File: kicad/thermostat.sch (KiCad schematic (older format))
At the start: 27 parts, among them IC1 LM2596S-5, J1 Display i2c, J2 Sensor i2c, J6 Screw_Terminal_01x05

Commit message: first pass at supercap circuit, still WIP
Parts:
- added C1: 25F, Capacitors_THT:CP_Radial_D16.0mm_P7.50mm, symbol Device:CP
- added C2: 2.2uF, Capacitors_SMD:C_0805, symbol Device:C
- added C3: 1nF, Capacitors_SMD:C_0805, symbol Device:C
- added C3: 100uF, Capacitors_SMD:C_0805, symbol Device:C
- added L2: 2.2uH, Inductors_SMD:L_Coilcraft_XAL5030, symbol Device:L
- added R10: 113k, Resistors_SMD:R_0805, symbol Device:R_US
- added R11: 38.3k, Resistors_SMD:R_0805, symbol Device:R_US
- added R12: 1k, Resistors_SMD:R_0805, symbol Device:R_US
- added R13: 348k, Resistors_SMD:R_0805, symbol Device:R_US
- added R14: 698k, Resistors_SMD:R_0805, symbol Device:R_US
- added R15: 1050k, Resistors_SMD:R_0805, symbol Device:R_US
- added R16: 200k, Resistors_SMD:R_0805, symbol Device:R_US
- added R18: 12m, Resistors_SMD:R_0805, symbol Device:R_US
- added U1: LTC4041, project_footprints:ltc4041, symbol thermostat:LTC4041
- added U2: SIR424DP, Housings_SOIC:PowerPAK_SO-8_Single, symbol thermostat:SIR424DP
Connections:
- net labels added: PWR_5V_BACKUP
- net labels removed: TEST
- wire segments 110 -> 149
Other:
- note added: "Need some kind of bypass mechanism"
- moved on the sheet: C1, C2, CONN1, D1, D2, D3, Gr1, IC1, J1, J2, J6, L1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

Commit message: addition of bmp280
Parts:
- added C21: 1uF, Capacitors_SMD:C_0805, symbol Device:C
- added C22: 100nF, Capacitors_SMD:C_0805, symbol Device:C
- added J31: Conn_02x03_Odd_Even, Socket_Strips:Socket_Strip_Straight_2x03_Pitch2.54mm_SMD, symbol Connector_Generic:Conn_02x03_Odd_Even
- added R21, R22, R23, R24: 10k, Resistors_SMD:R_0805, symbol Device:R_US
- added U21: BMP280, Housings_LGA:Bosch_LGA-8_2.5x2.5mm_Pitch0.65mm_ClockwisePinNumbering, symbol Sensor_Pressure:BMP280
- IC1: footprint project_footprints:TO170P1435X465-6N -> TO_SOT_Packages_SMD:TO-263-5_TabPin3
- RELAY1, RELAY2, RELAY3: symbol thermostat:Relay? -> thermostat-rescue:Relay?-thermostat
- U11: renamed from U1; Mouser 584-4041IUFDPB -> 584-4041EUFDPB
- renumbered C1 to C11, C2 to C12, C3 to C13, C3 to C14, U2 to U12
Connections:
- net labels added: PWR_5V_CAP, PWR_5V_CAP_IN, PWR_5V_RAW
- net labels removed: PWR_5V_BACKUP
- wire segments 149 -> 182
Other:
- note added: "Based on https://www.electroschematics.com/bmp280-diy-project-primer/"
- note added: "To bypass supercapacitor circuit, jumper 1,2\nTo enable supercapacitor circuit, jumper 3,4 and 5,6"
- note removed: "Need some kind of bypass mechanism"
- moved on the sheet: C1, C11, C12, C13, C14, C2, D1, D2, D3, Gr1, IC1, L1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

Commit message: updates
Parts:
- removed J2: Sensor i2c, Socket_Strips:Socket_Strip_Straight_1x04_Pitch2.54mm, symbol Connector_Generic:Conn_01x04
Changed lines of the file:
@@
 	1700 1100 1700 750
 Connection ~ 1700 1100
-Text Label 2100 3200 0    50   ~ 0
-GND
 Wire Wire Line
 	2500 2700 2500 3200
@@
 	1800 3000 1800 3200
 Wire Wire Line
-	1800 3200 2500 3200
+	1800 3200 2150 3200
 Text Label 6600 1400 0    50   ~ 0
 HVAC_PWR(RED)
@@
 	1    0    0    -1
 $EndComp
-$Comp
-L Connector_Generic:Conn_01x04 J2
-U 1 1 5D67AFA8
-P 7600 2650
-F 0 "J2" H 7680 2642 50  0000 L CNN
-F 1 "Sensor i2c" H 7680 2551 50  0000 L CNN
-F 2 "Socket_Strips:Socket_Strip_Straight_1x04_Pitch2.54mm" H 7600 2650 50  0001 C CNN
-F 3 "~" H 7600 2650 50  0001 C CNN
-F 4 "99" H 7600 2650 50  0001 C CNN "Populate"
-F 5 "200-SLW10401SS" H 7600 2650 50  0001 C CNN "Mouser"
-	1    7600 2650
-	1    0    0    -1
-$EndComp
 Text Label 7200 2050 2    50   ~ 0
 GND
@@
 Text Label 7200 2350 2    50   ~ 0
 GPIO3(SCL1)
-Text Label 7200 2550 2    50   ~ 0
-GPIO2(SDA1)
-Text Label 7200 2650 2    50   ~ 0
-GPIO3(SCL1)
-Text Label 7200 2750 2    50   ~ 0
-GND
-Text Label 7200 2850 2    50   ~ 0
-PWR_5V
 Wire Wire Line
 	7200 2050 7400 2050
@@
 Wire Wire Line
 	7200 2350 7400 2350
-Wire Wire Line
-	7400 2550 7200 2550
-Wire Wire Line
-	7400 2650 7200 2650
-Wire Wire Line
-	7200 2750 7400 2750
-Wire Wire Line
-	7400 2850 7200 2850
 $Comp
 L thermostat:LM2596S-12-RENUM IC1
@@
 	9400 4450 9500 4450
 Connection ~ 9500 4450
-Text Label 9500 3500 2    50   ~ 0
+Text Label 9500 3400 2    50   ~ 0
 PWR_3.3V
 Text Label 8500 4300 3    50   ~ 0
@@
 	9500 3550 10100 3550
 Wire Wire Line
-	9500 3500 9500 3550
-Wire Wire Line
 	9400 3700 9400 3550
 Connection ~ 9400 3550
@@
 	8500 4300 8500 4000
 Connection ~ 8500 4000
-Text Notes 7750 3400 0    50   ~ 0
+Text Notes 7750 3300 0    50   ~ 0
 Based on https://www.electroschematics.com/bmp280-diy-project-primer/
+$Comp
+L thermostat:GND #PWR?
+U 1 1 5E0DA227
+P 2150 3200
+F 0 "#PWR?" H 2150 2950 50  0001 C CNN
+F 1 "GND" H 2155 3027 50  0000 C CNN
+F 2 "" H 2150 3200 50  0000 C CNN
+F 3 "" H 2150 3200 50  0000 C CNN
+	1    2150 3200
+	1    0    0    -1
+$EndComp
+Wire Wire Line
+	2150 3200 2500 3200
+Connection ~ 2150 3200
+Wire Wire Line
+	9500 3400 9500 3550
 $EndSCHEMATC

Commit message: new symbol for transistor
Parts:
- removed U12: SIR424DP, Housings_SOIC:PowerPAK_SO-8_Single, symbol thermostat:SIR424DP
- added T1: SIR424DP, Housings_SOIC:PowerPAK_SO-8_Single, symbol Transistor_FET:BUK9M9R1-40EX
- U11: symbol thermostat:LTC4041 -> thermostat-rescue:LTC4041-thermostat
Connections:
- net PWR_5V_CAP: now also T1.5 (D)
- net at U11.15 (IGATE): now also T1.4 (G)
- net at R18.1, U11.7 (CLN): now also T1.1 (S), T1.2 (S), T1.3 (S)
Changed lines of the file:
@@
 EESchema Schematic File Version 4
-LIBS:thermostat-cache
-EELAYER 29 0
+EELAYER 30 0
 EELAYER END
 $Descr A4 11693 8268
@@
 	2850 5450 2950 5450
 $Comp
-L thermostat:LTC4041 U11
+L thermostat-rescue:LTC4041-thermostat U11
 U 1 1 5E1374C4
 P 2500 6250
@@
 Wire Wire Line
 	2550 5150 2550 5450
-Connection ~ 2550 5150
 Wire Wire Line
 	2950 5450 3200 5450
 Wire Wire Line
 	3200 5450 3200 5150
-Wire Wire Line
-	3200 5150 3050 5150
 Connection ~ 2950 5450
 Wire Wire Line
 	3200 5150 3400 5150
 Connection ~ 3200 5150
-Wire Wire Line
-	2700 5400 2700 5450
-Wire Wire Line
-	3050 5250 3050 5150
-Connection ~ 3050 5150
-$Comp
-L thermostat:SIR424DP U12
-U 1 1 5E21048A
-P 2900 5200
-F 0 "U12" H 2750 5450 50  0000 L CNN
-F 1 "SIR424DP" H 2600 5350 50  0000 L CNN
-F 2 "Housings_SOIC:PowerPAK_SO-8_Single" V 2750 4950 50  0001 C CNN
-F 3 "https://www.mouser.com/datasheet/2/427/sir424dp-244427.pdf" H 2900 5250 50  0001 C CNN
-F 4 "781-SIR424DP-GE3" V 2850 5200 50  0001 C CNN "Mouser"
-	1    2900 5200
-	1    0    0    -1
-$EndComp
 $Comp
 L Device:R_US R10
@@
 Wire Wire Line
 	9500 3400 9500 3550
+$Comp
+L Transistor_FET:BUK9M9R1-40EX T1
+U 1 1 5E0E0418
+P 2750 5250
+F 0 "T1" V 3092 5250 50  0000 C CNN
+F 1 "SIR424DP" V 3001 5250 50  0000 C CNN
+F 2 "Housings_SOIC:PowerPAK_SO-8_Single" H 2950 5175 50  0001 L CIN
+F 3 "https://www.mouser.com/datasheet/2/427/sir424dp-244427.pdf" V 2750 5250 50  0001 L CNN
+F 4 "781-SIR424DP-GE3" H 2750 5250 50  0001 C CNN "Mouser"
+	1    2750 5250
+	0    1    -1   0
+$EndComp
+Connection ~ 2550 5150
+Wire Wire Line
+	2700 5450 2750 5450
+Wire Wire Line
+	2950 5150 3200 5150
 $EndSCHEMATC

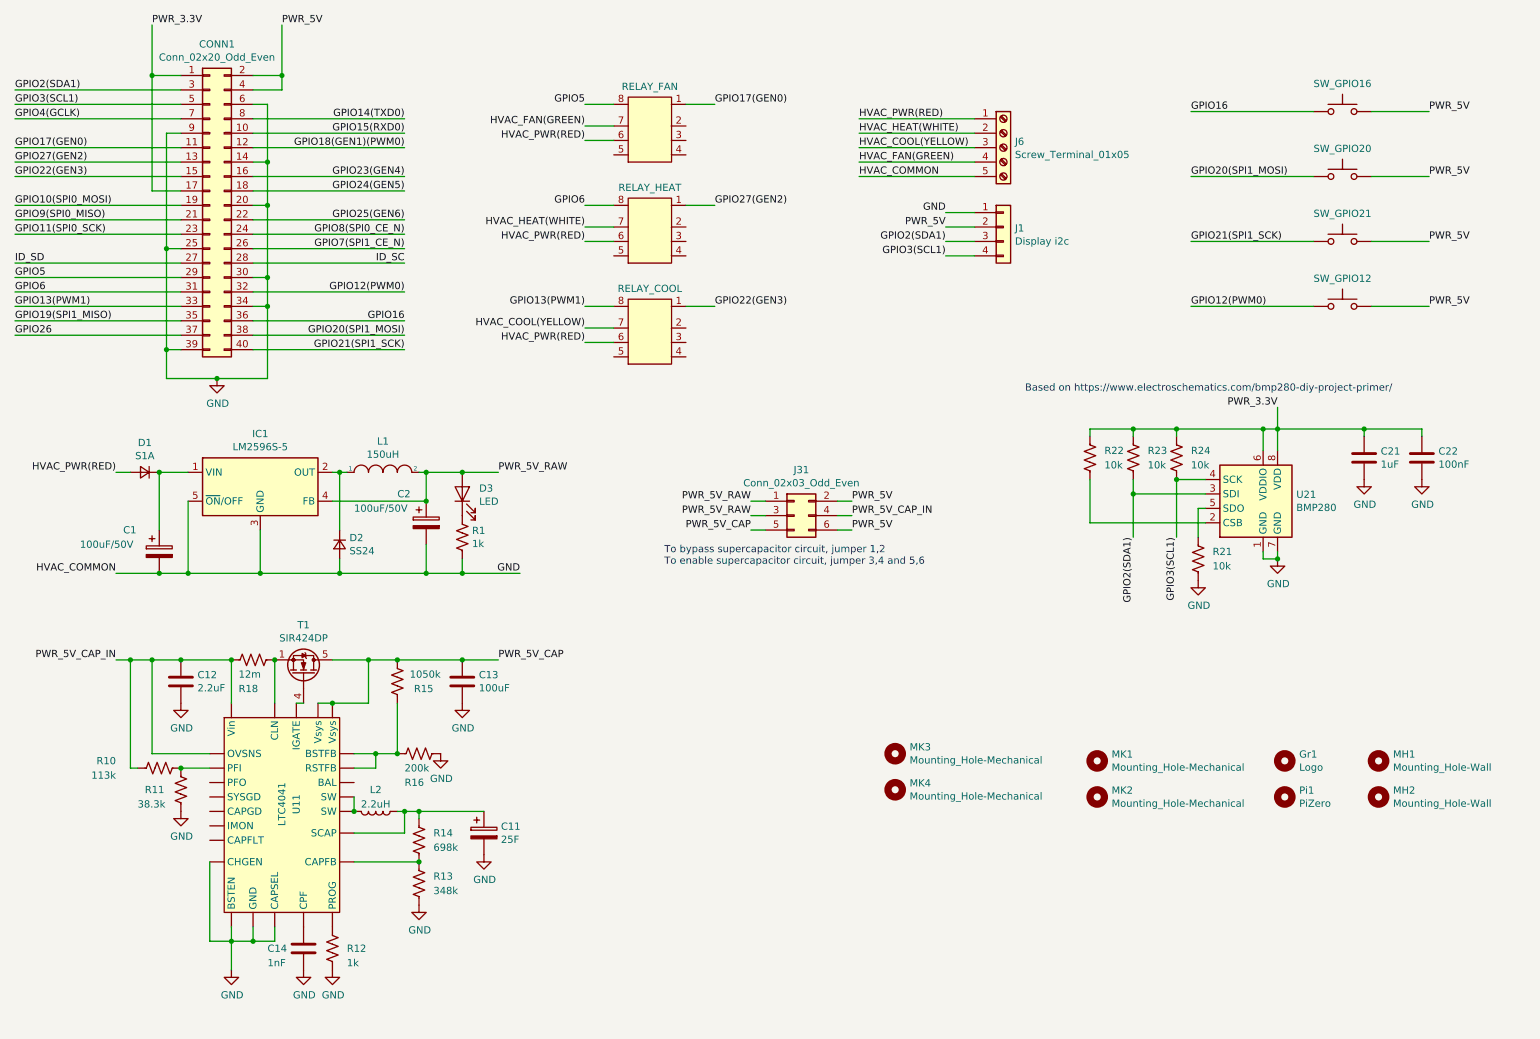
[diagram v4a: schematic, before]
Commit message: Support for KiCad v5.14 libraries
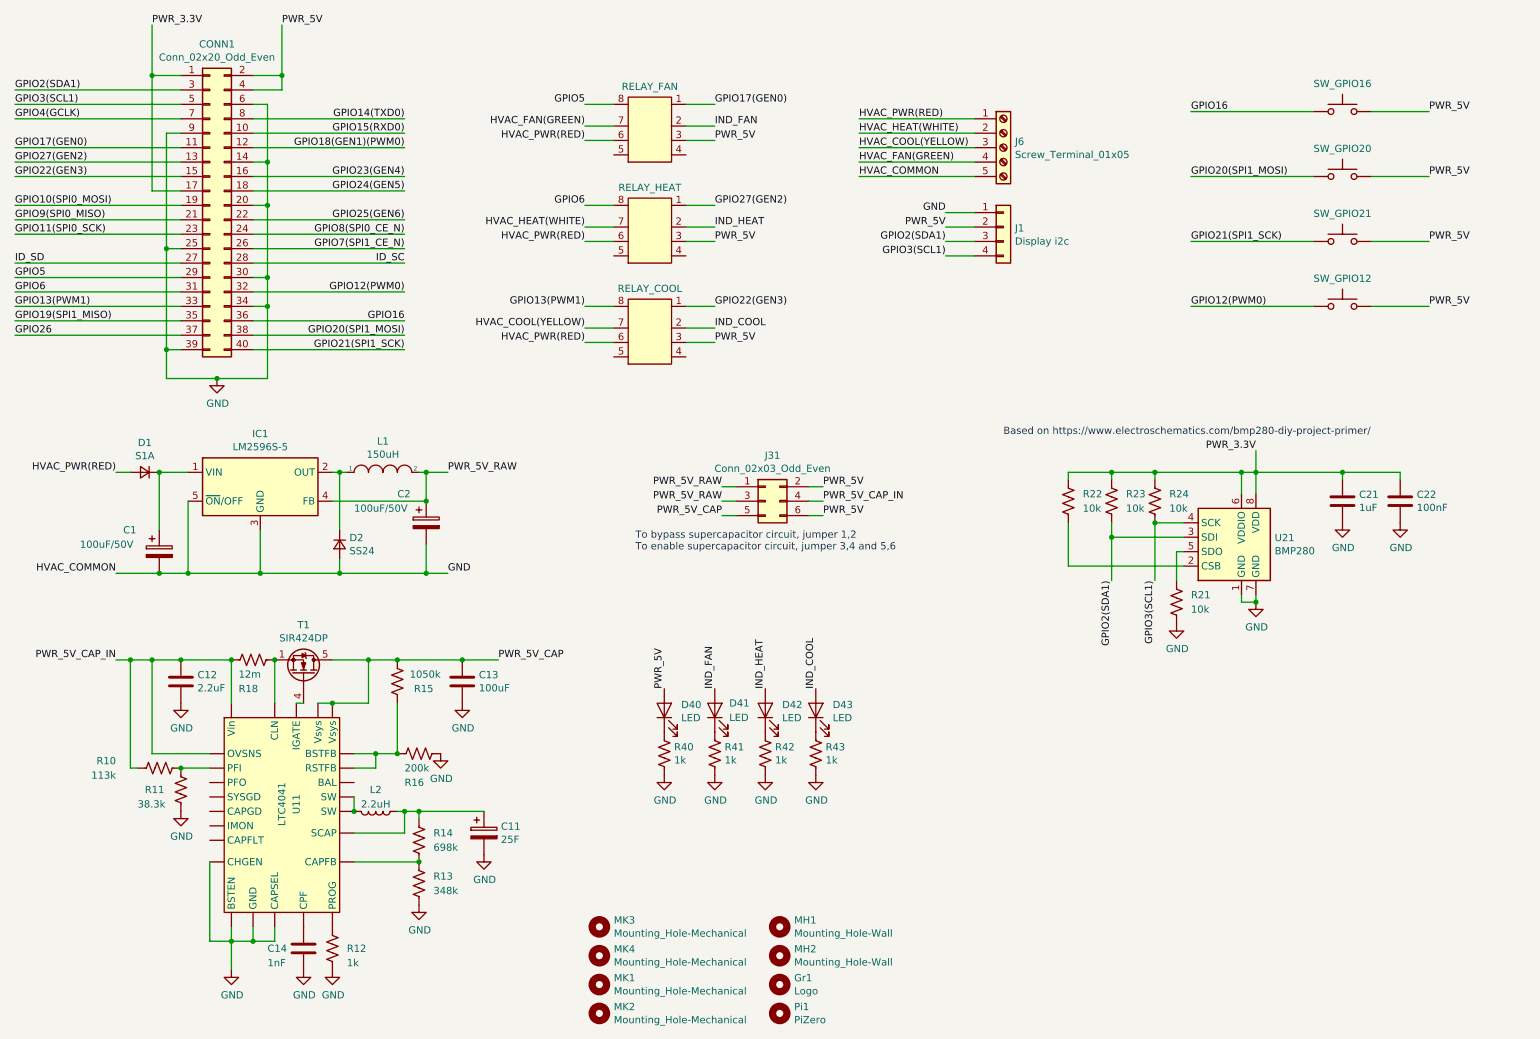
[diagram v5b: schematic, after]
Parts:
- added D41, D42, D43: LED, LED_SMD:LED_0805_2012Metric, symbol Device:LED
- added R41, R42, R43: 1k, Resistor_SMD:R_0805_2012Metric, symbol Device:R_US
- C11: footprint Capacitors_THT:CP_Radial_D16.0mm_P7.50mm -> Capacitor_THT:C_Radial_D16.0mm_H31.5mm_P7.50mm
- C12, C13, C14, C21, C22: footprint Capacitors_SMD:C_0805 -> Capacitor_SMD:C_0805_2012Metric
- D40: renamed from D3; footprint LEDs:LED_0805 -> LED_SMD:LED_0805_2012Metric
- IC1: footprint TO_SOT_Packages_SMD:TO-263-5_TabPin3 -> Package_TO_SOT_SMD:TO-263-5_TabPin3
- J31: footprint Socket_Strips:Socket_Strip_Straight_2x03_Pitch2.54mm_SMD -> Connector_PinHeader_2.54mm:PinHeader_2x03_P2.54mm_Vertical_SMD
- L2: footprint Inductors_SMD:L_Coilcraft_XAL5030 -> Inductor_SMD:L_Coilcraft_XAL5030
- R10, R11, R12, R13, R14, R15, R16, R18, R21, R22, R23, R24: footprint Resistors_SMD:R_0805 -> Resistor_SMD:R_0805_2012Metric
- R40: renamed from R1; footprint Resistors_SMD:R_0805 -> Resistor_SMD:R_0805_2012Metric
- T1: footprint Housings_SOIC:PowerPAK_SO-8_Single -> Package_SO:PowerPAK_SO-8_Single
- U21: footprint Housings_LGA:Bosch_LGA-8_2.5x2.5mm_Pitch0.65mm_ClockwisePinNumbering -> Package_LGA:Bosch_LGA-8_2x2.5mm_P0.65mm_ClockwisePinNumbering
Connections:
- net GND: now also R41.2, R42.2, R43.2
- net PWR_5V: now also D40.2 (A), RELAY1.3, RELAY2.3, RELAY3.3
- net PWR_5V_RAW: no longer D40.2 (A)
- net IND_FAN: now reaches RELAY1.2
- net IND_FAN: now also D41.2 (A)
- net IND_HEAT: now reaches RELAY2.2
- net IND_HEAT: now also D42.2 (A)
- net IND_COOL: now reaches RELAY3.2
- net IND_COOL: now also D43.2 (A)
- new net: D41.1 (K), R41.1
- new net: D42.1 (K), R42.1
- new net: D43.1 (K), R43.1
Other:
- moved on the sheet: C21, C22, D40, Gr1, J31, MH1, MH2, MK1, MK2, MK3, MK4, Pi1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
